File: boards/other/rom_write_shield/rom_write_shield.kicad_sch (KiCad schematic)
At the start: 38 parts, among them J1 Conn_01x08, J2 Conn_01x06, J3 Conn_01x08, J4 Conn_01x06, J5 Conn_02x10_Top_Bottom, J6 Conn_01x02, J7 vraw_test, Q1 2SC1815, U1 LT1930, U2 LM358N

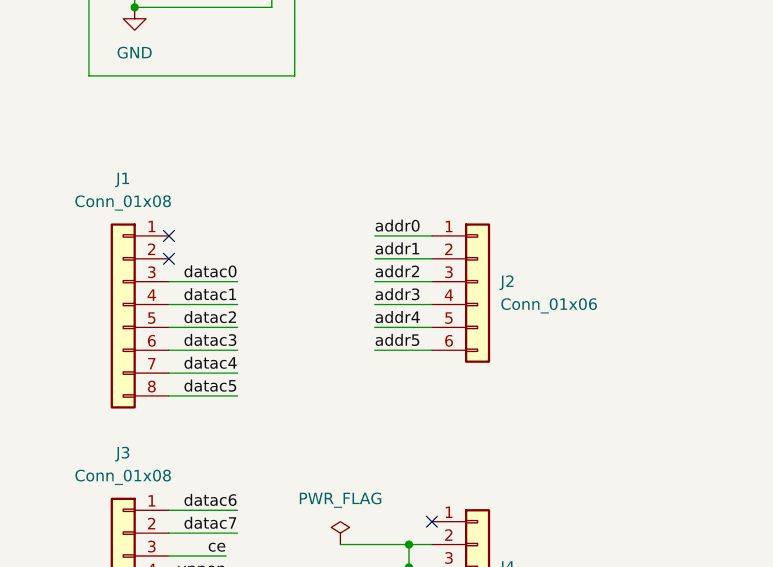
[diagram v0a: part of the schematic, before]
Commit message: fix rom_write_shield and convenient_port_shield
fix reversed Arduino analog ports
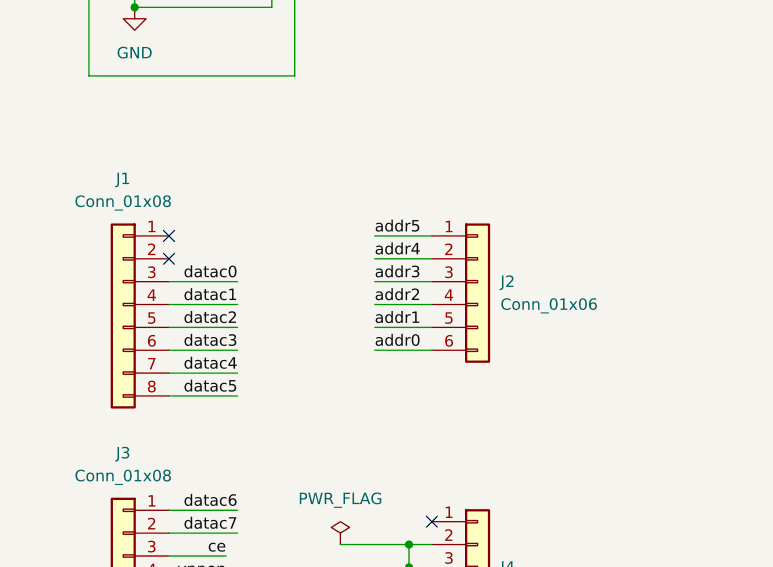
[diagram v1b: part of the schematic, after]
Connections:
- net addr0: now also J2.6 (Pin_6); no longer J2.1 (Pin_1)
- net addr1: now also J2.5 (Pin_5); no longer J2.2 (Pin_2)
- net addr2: now also J2.4 (Pin_4); no longer J2.3 (Pin_3)
- net addr3: now also J2.3 (Pin_3); no longer J2.4 (Pin_4)
- net addr4: now also J2.2 (Pin_2); no longer J2.5 (Pin_5)
- net addr5: now also J2.1 (Pin_1); no longer J2.6 (Pin_6)
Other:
- title: (none) -> EPROM Programming Shield
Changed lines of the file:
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@@
 (kicad_sch (version 20211123) (generator eeschema)
   (paper "A4")
+  (title_block
+    (title "EPROM Programming Shield")
+    (rev "v1.1")
+  )
   (junction (at 121.92 59.055) (diameter 0) (color 0 0 0 0)
   )
@@
     (effects (font (size 1.27 1.27)) (justify left bottom))
   )
-  (label "addr4" (at 232.41 113.03 0)
+  (label "addr1" (at 232.41 113.03 0)
     (effects (font (size 1.27 1.27)) (justify left bottom))
   )
@@
     (effects (font (size 1.27 1.27)) (justify left bottom))
   )
-  (label "addr0" (at 232.41 102.87 0)
+  (label "addr5" (at 232.41 102.87 0)
     (effects (font (size 1.27 1.27)) (justify left bottom))
   )
@@
     (effects (font (size 1.27 1.27)) (justify right bottom))
   )
-  (label "addr1" (at 232.41 105.41 0)
+  (label "addr4" (at 232.41 105.41 0)
     (effects (font (size 1.27 1.27)) (justify left bottom))
   )
@@
     (effects (font (size 1.27 1.27)) (justify right bottom))
   )
-  (label "addr5" (at 232.41 115.57 0)
+  (label "addr0" (at 232.41 115.57 0)
     (effects (font (size 1.27 1.27)) (justify left bottom))
   )
@@
     (effects (font (size 1.27 1.27)) (justify left bottom))
   )
-  (label "addr3" (at 232.41 110.49 0)
+  (label "addr2" (at 232.41 110.49 0)
     (effects (font (size 1.27 1.27)) (justify left bottom))
   )
@@
     (effects (font (size 1.27 1.27)) (justify left bottom))
   )
-  (label "addr2" (at 232.41 107.95 0)
-    (effects (font (size 1.27 1.27)) (justify left bottom))
-  )
+  (label "addr3" (at 232.41 107.95 0)
+    (effects (font (size 1.27 1.27)) (justify left bottom))
+  )
